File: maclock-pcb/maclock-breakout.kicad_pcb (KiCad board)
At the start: 2 copper layers, 70.5 x 26.5 mm, 10 parts, among them SW1 TS32735BK160RASMTTR, SW2 TS32735BK160RASMTTR

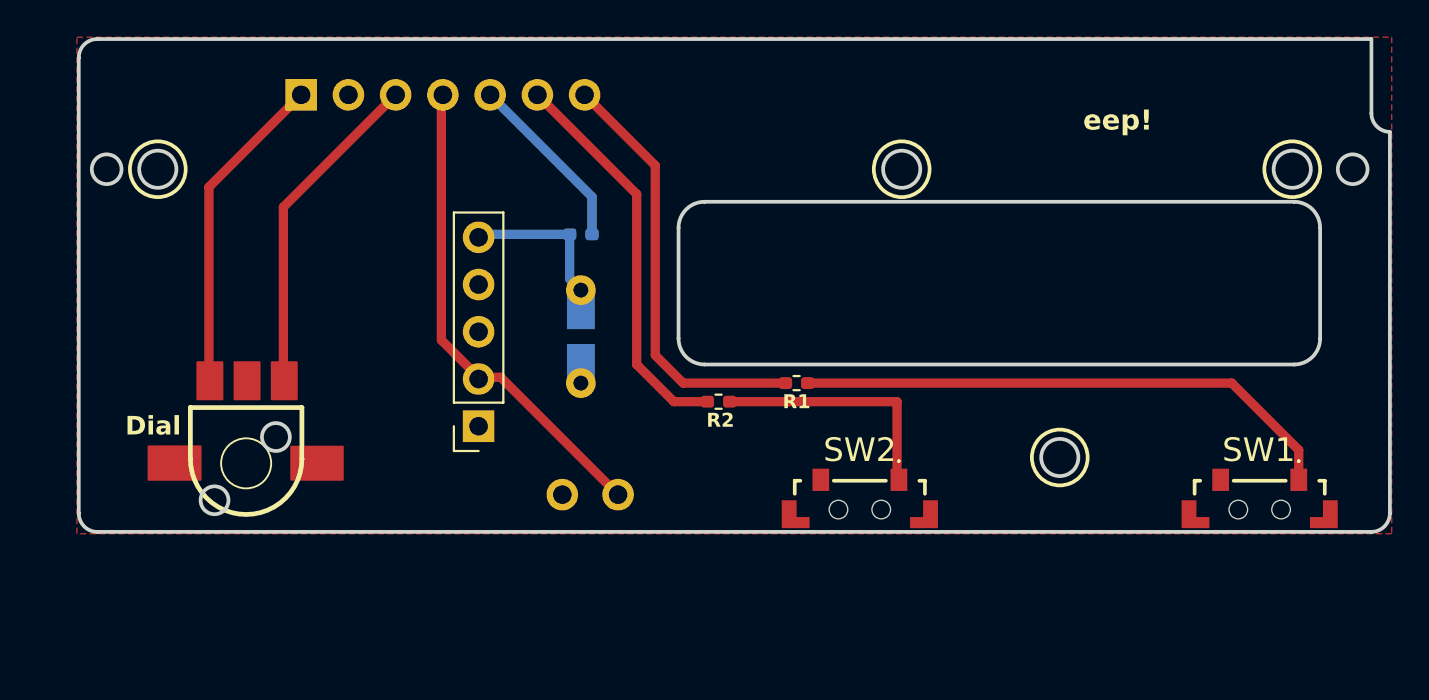
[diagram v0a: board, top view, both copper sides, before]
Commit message: PCB: real SW/encoder footprints, SMD 1206 C1, JST headers, amp decoupling
- SW1/SW2: hand-made TS32 land -> real maclock:SW_Push_5x7.8x3.8mm_SMD, same
  placement; value TS32-7-35-BK-160-RA-SMT-TR
- ENC1: fake 'Dial' copper -> real E8E8-3.2C60-9B34 encoder footprint, pads
  netted (ENC_A/ENC_B/GND)
- C1: hybrid disc/chip land now SMD-classed with a 1206 chip 3D model (100nF)
- J1/J2: JST ZH 2-pin/4-pin vertical connectors (wiring in progress)
- C2/C3: 10uF + 100nF decoupling at the PAM8302 Vin (JP1)
- README BOM updated; new maclock.pretty footprint library
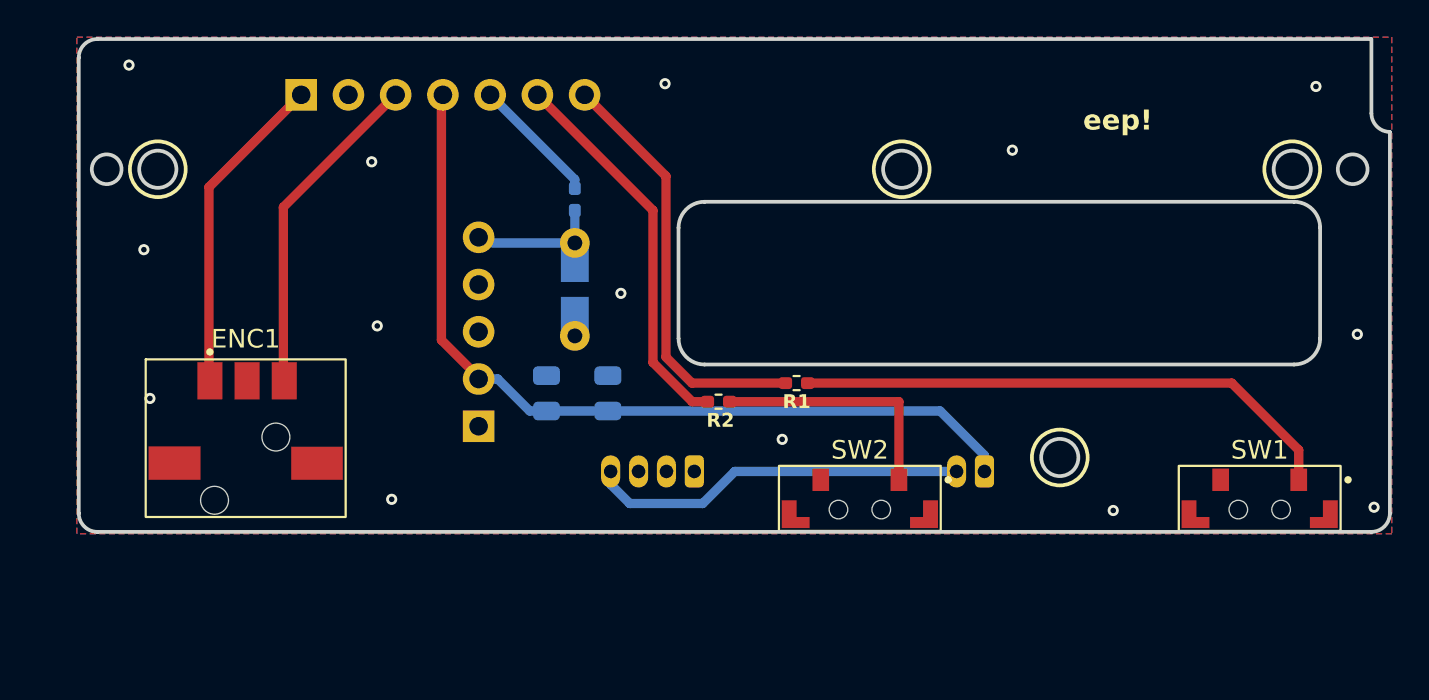
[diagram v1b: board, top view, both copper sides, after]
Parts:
- removed BAT+: 5V, 
- removed BAT-: GND, 
- added C2: 100nF, Capacitor_SMD:C_0805_2012Metric, B.Cu at (145.9, 97.0)
- added C3: 10uF, Capacitor_SMD:C_0805_2012Metric, B.Cu at (142.7, 97.0)
- added ENC1: E8E8-3.2C60-9B34, maclock:RotaryEncoder_E8E8-3.2C60-9B34_SMD, F.Cu at (126.5, 100.0)
- added J1: JST_ZH_B2B-ZR_1x02_P1.50mm_Vertical, Connector_JST:JST_ZH_B2B-ZR_1x02_P1.50mm_Vertical, B.Cu at (166.2, 101.2)
- added J2: JST_ZH_B4B-ZR_1x04_P1.50mm_Vertical, Connector_JST:JST_ZH_B4B-ZR_1x04_P1.50mm_Vertical, B.Cu at (150.6, 101.2)
- C1: footprint Capacitor_THT:C_Disc_D6.0mm_W2.5mm_P5.00mm -> maclock:C_Chip_or_Disc_P5mm_SMD
- JP1: moved to B.Cu
- SW1, SW2: value TS32735BK160RASMTTR -> TS32-7-35-BK-160-RA-SMT-TR; footprint KiCad:TS32735BK160RASMTTR -> maclock:SW_Push_5x7.8x3.8mm_SMD
- moved C1 2.56 mm to (144.2, 94.0)
- moved R3 1.90 mm to (144.2, 86.6), turned to 90 degrees
- turned JP1 to 0 degrees
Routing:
- net 5V_IN: track 0.00 -> 20.4 mm
- net 5V: track 26.1 -> 45.7 mm
- net AUDIO: track 18.1 -> 14.0 mm
- net BTN2: track 34.6 -> 34.1 mm
- net GND: vias 0 -> 14
- added copper zone on B.Cu, net GND
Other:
- outline, holes or cut-outs redrawn
- board text added: "rev 2026.09"
- board text removed: "Dial"
- board text removed: "Input"
- board text removed: "rev 2026.05"

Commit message: PCB: real HYCW03 encoder, LCSC-sourceable BOM, rebuilt schematic
- ENC1: F-Switch E8E8-3.2C60-9B34 (not on LCSC) -> HOAUC HYCW03-2.8D-5P-S
  (C55218995); new footprint, bore placed 8.8mm from the left edge / 4mm from
  the bottom to keep the dial aligned with the case
- Nets: split the series-resistor button nets (BTN1/SW1, BTN2/SW2) so each is
  fully connected; assigned ENC1 pad nets; normalized all board nets to the
  /-prefixed hierarchical form to match the schematic
- Rebuilt maclock-breakout.kicad_sch from the PCB (was a PiInput-only stub):
  all 11 parts with correct footprints/values/LCSC, custom ENC1 symbol in
  maclock.kicad_sym; ERC 0/0, board<->schematic parity clean but for benign
  symbol metadata
- BOM: every part now resolves to an LCSC number (added J1 C158011, J2 C157997);
  PCBWAY_REPLY.md answers the quote's four flagged parts
- Switches: added TS24CA and TSB001 side-switch footprints as LCSC-stocked
  alternatives to the Same Sky TS32; board left on the TS32 for hand-positioning
- scripts/: reproducible pcbnew edits (bundled Python) for each board change
- README: BOM, sourcing, J1 power switch / J2 power input, schematic status
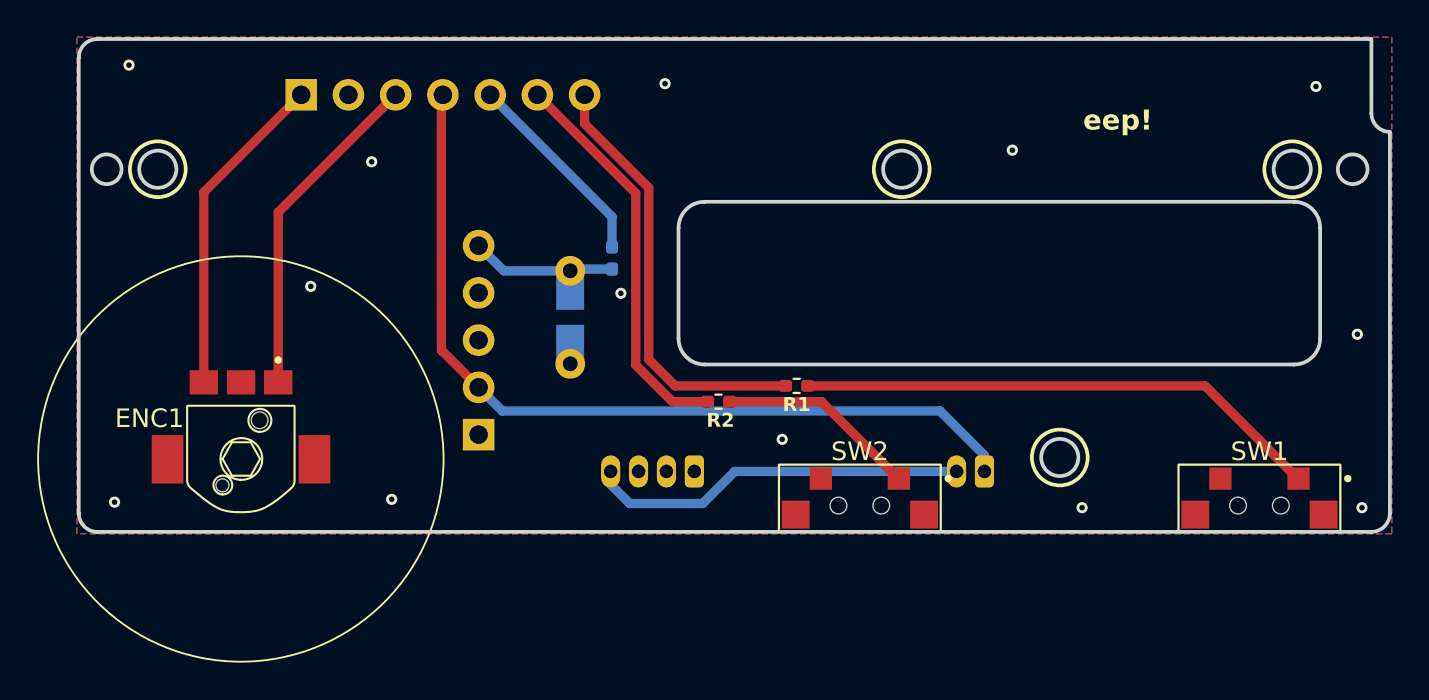
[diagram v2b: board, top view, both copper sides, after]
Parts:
- removed C2: 100nF, Capacitor_SMD:C_0805_2012Metric
- removed C3: 10uF, Capacitor_SMD:C_0805_2012Metric
- ENC1: value E8E8-3.2C60-9B34 -> HYCW03-2.8D-5P-S; footprint maclock:RotaryEncoder_E8E8-3.2C60-9B34_SMD -> maclock:RotaryEncoder_HYCW03-2.8D-5P-S_SMD
- JP1: value Rotary_Encoder_5pin -> PAM8302_Socket_1x5
- SW1, SW2: value TS32-7-35-BK-160-RA-SMT-TR -> SW_TSB001_7.7x3.55_SideSMD; footprint maclock:SW_Push_5x7.8x3.8mm_SMD -> maclock:SW_TSB001_7.7x3.55_SideSMD
- moved R3 3.73 mm to (146.2, 89.8), turned to -90 degrees
- moved SW1 1.65 mm to (181.0, 102.6)
- moved SW2 1.64 mm to (159.5, 102.6)
- moved C1 1.52 mm to (143.9, 95.5)
- moved ENC1 1.50 mm to (126.2, 98.5), turned to 180 degrees
- moved JP1 0.45 mm to (139.0, 99.3)
- moved R1 0.15 mm to (156.1, 96.7)
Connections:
- net 5V renamed /5V
- net 5V_IN renamed /5V_IN
- C1 pad 1: GND -> /GND
- C1 pad 2: AUDIO -> /A+
- ENC1 pad 4: GND -> /GND
- ENC1 pad 5: GND -> /GND
- J2 pad 3: GND -> /GND
- JP1 pad 1: GND -> /GND
- JP1 pad 4: GND -> /GND
- JP1 pad 5: AUDIO -> /A+
- PiInput pad 1: ENC_B -> /ENC_B
- PiInput pad 2: GND -> /GND
- PiInput pad 3: ENC_A -> /ENC_A
- PiInput pad 5: AUDIO -> /AUDIO
- PiInput pad 6: BTN2 -> /BTN2
- PiInput pad 7: BTN1 -> /BTN1
- R1 pad 1: BTN1 -> /BTN1
- R1 pad 2: BTN1 -> /SW1
- R2 pad 1: BTN2 -> /BTN2
- R2 pad 2: BTN2 -> /SW2
- R3 pad 1: AUDIO -> /AUDIO
- R3 pad 2: AUDIO -> /A+
- SW1 pad 1: BTN1 -> /SW1
- SW1 pad 2: GND -> /GND
- SW1 pad 3: GND -> /GND
- SW1 pad 4: GND -> /GND
- SW2 pad 1: BTN2 -> /SW2
- SW2 pad 2: GND -> /GND
- SW2 pad 3: GND -> /GND
- SW2 pad 4: GND -> /GND
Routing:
- net BTN1: track 52.4 -> 0.00 mm
- net BTN2: track 34.1 -> 0.00 mm
- net /SW1: track 0.00 -> 28.3 mm
- net /BTN1: track 0.00 -> 23.6 mm
- net /BTN2: track 0.00 -> 21.4 mm
- net /ENC_A: track 0.00 -> 18.1 mm
- net /ENC_B: track 0.00 -> 17.6 mm
- net ENC_A: track 17.5 -> 0.00 mm
- net ENC_B: track 17.1 -> 0.00 mm
- net AUDIO: track 14.0 -> 0.00 mm
- net /AUDIO: track 0.00 -> 10.9 mm
- net /SW2: track 0.00 -> 10.8 mm
- net /A+: track 0.00 -> 7.77 mm
- net GND: vias 14 -> 0
- net /GND: vias 0 -> 13
- added copper zone on B.Cu, net /GND
- added copper zone on F.Cu, net /GND
- removed copper zone on B.Cu, net GND
- removed copper zone on F.Cu, net GND
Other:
- board text added: "by Wells Workshop - https://wells.ee"
- board text removed: "Designed by Wells Riley •https://wells.ee"

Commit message: PCB: TSB001 part numbers on board, C1 10nF audio LPF, J2 polarity silk, project lib tables, C1 1206 model
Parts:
- C1: value 100nF -> 10nF
- SW1, SW2: value SW_TSB001_7.7x3.55_SideSMD -> TSB001A3518A
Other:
- board text added: "+"
- board text added: "-"
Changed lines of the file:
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@@
 			)
 		)
-		(property "Value" "SW_TSB001_7.7x3.55_SideSMD"
+		(property "Value" "TSB001A3518A"
 			(at 0 2.82 0)
 			(layer "F.Fab")
@@
 			)
 		)
+		(property "LCSC" "C2888448"
+			(at 0 0 0)
+			(layer "F.SilkS")
+			(hide yes)
+			(effects
+				(font
+					(size 1.27 1.27)
+					(thickness 0.15)
+				)
+			)
+		)
 		(attr smd)
 		(duplicate_pad_numbers_are_jumpers no)
@@
 			)
 		)
-		(property "Value" "SW_TSB001_7.7x3.55_SideSMD"
+		(property "Value" "TSB001A3518A"
 			(at 0 2.82 0)
 			(layer "F.Fab")
@@
 			)
 		)
+		(property "LCSC" "C2888448"
+			(at 0 0 0)
+			(layer "F.SilkS")
+			(hide yes)
+			(effects
+				(font
+					(size 1.27 1.27)
+					(thickness 0.15)
+				)
+			)
+		)
 		(attr smd)
 		(duplicate_pad_numbers_are_jumpers no)
@@
 			)
 		)
-		(property "Value" "100nF"
+		(property "Value" "10nF"
 			(at 2.5 -2.05 270)
 			(layer "B.Fab")
@@
 			)
 		)
-		(property "LCSC" "C24497"
+		(property "LCSC" "C1846"
 			(at 0 0 0)
 			(layer "B.SilkS")
@@
 		)
 		(embedded_fonts no)
-		(model "${KICAD9_3DMODEL_DIR}/Capacitor_SMD.3dshapes/C_0402_1005Metric.step"
+		(model "${KICAD10_3DMODEL_DIR}/Capacitor_SMD.3dshapes/C_1206_3216Metric.step"
 			(offset
 				(xyz 2.5 0 0)
@@
 		)
 	)
+	(gr_text "+"
+		(at 146.1 99.15 0)
+		(layer "B.SilkS")
+		(effects
+			(font
+				(size 0.8 0.8)
+				(thickness 0.15)
+			)
+			(justify mirror)
+		)
+	)
+	(gr_text "-"
+		(at 147.6 99.15 0)
+		(layer "B.SilkS")
+		(effects
+			(font
+				(size 0.8 0.8)
+				(thickness 0.15)
+			)
+			(justify mirror)
+		)
+	)
 	(gr_text "Pi GPIO"
 		(at 127.5 81 0)
@@
 		(layer "B.SilkS")
 	)
+	(segment
+		(start 178.0625 96.65)
+		(end 156.845 96.65)
+		(width 0.5)
+		(layer "F.Cu")
+		(net "/SW1")
+	)
+	(segment
+		(start 183.0875 101.675)
+		(end 178.0625 96.65)
+		(width 0.5)
+		(layer "F.Cu")
+		(net "/SW1")
+	)
 	(via
 		(at 186.25 93.875)
@@
 	)
 	(segment
+		(start 152.5 97.5)
+		(end 157.445 97.5)
+		(width 0.5)
+		(layer "F.Cu")
+		(net "/SW2")
+	)
+	(segment
+		(start 157.445 97.5)
+		(end 161.6 101.655)
+		(width 0.5)
+		(layer "F.Cu")
+		(net "/SW2")
+	)
+	(segment
 		(start 149.425 97.5)
 		(end 151.305 97.5)
@@
 	)
 	(segment
-		(start 152.5 97.5)
-		(end 157.445 97.5)
-		(width 0.5)
-		(layer "F.Cu")
-		(net "/SW2")
-	)
-	(segment
-		(start 157.445 97.5)
-		(end 161.6 101.655)
-		(width 0.5)
-		(layer "F.Cu")
-		(net "/SW2")
-	)
-	(segment
-		(start 178.0625 96.65)
-		(end 156.845 96.65)
-		(width 0.5)
-		(layer "F.Cu")
-		(net "/SW1")
-	)
-	(segment
-		(start 183.0875 101.675)
-		(end 178.0625 96.65)
-		(width 0.5)
-		(layer "F.Cu")
-		(net "/SW1")
-	)
-	(segment

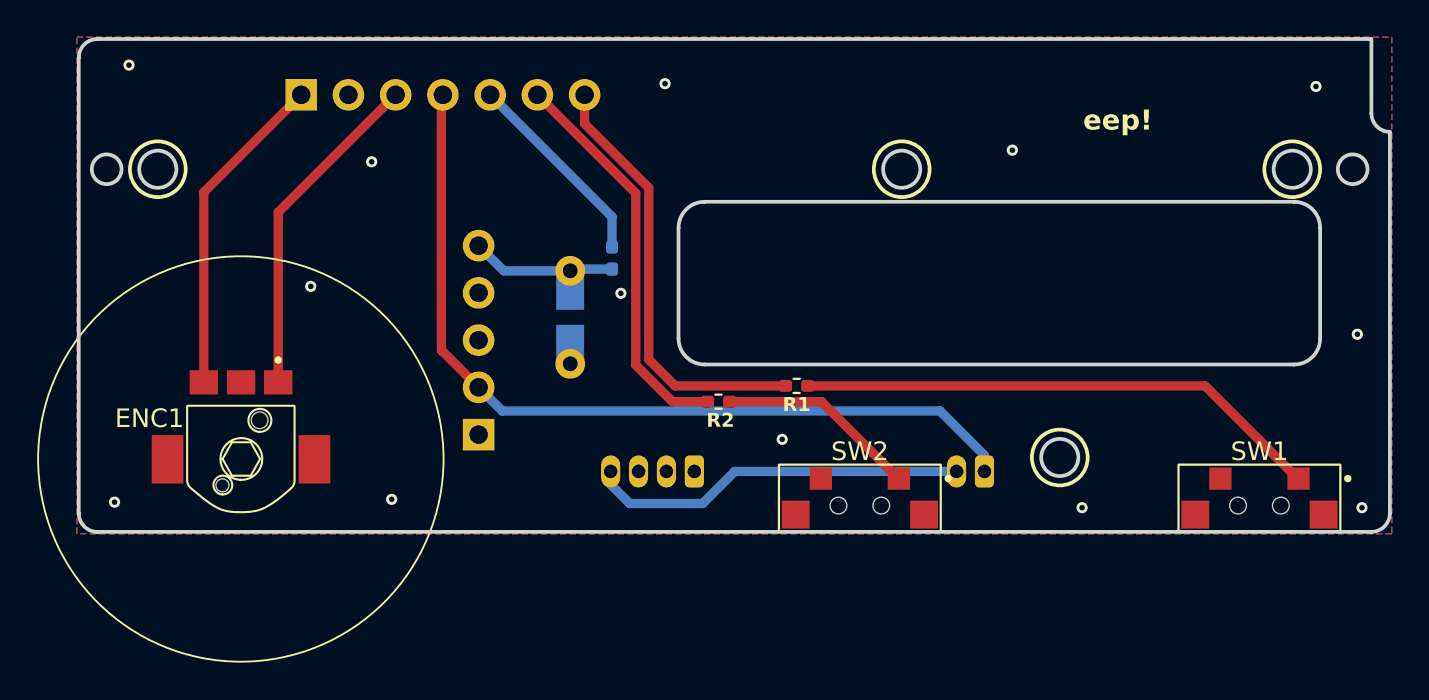
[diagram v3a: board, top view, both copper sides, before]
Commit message: PCB: connector MPN values, 1.0 mm 5V supply tracks
- J1/J2/JP1/PiInput Value -> B2B-ZR(LF)(SN) / B4B-ZR(LF)(SN) / 2.54-1*5PFemale / PZ254V-11-07P
  on board and schematic (PCBway reads the board's Value column)
- /5V and /5V_IN tracks 0.5 -> 1.0 mm; the J2 pad-1 skirt is 0.8 mm and the diagonal out of
  JP1 pin 2 stays 0.5 mm (2.54 mm socket pitch); long y=98 run restarted at x=141 with a stub
  so its round end clears JP1 pin 1 (GND)
- DRC 0 errors / 0 unconnected; ERC 0; scripts/mpn_values_and_wide_5v.py
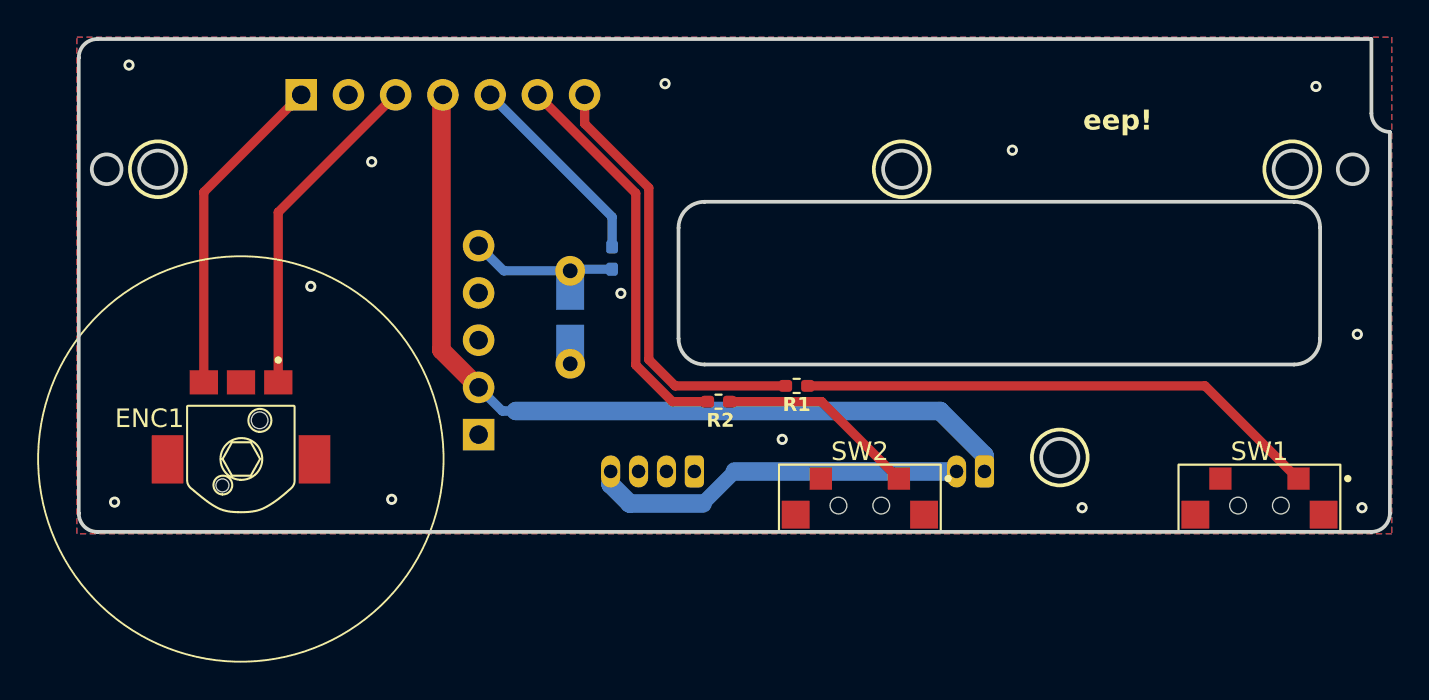
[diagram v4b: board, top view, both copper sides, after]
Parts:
- J1: value JST_ZH_B2B-ZR_1x02_P1.50mm_Vertical -> B2B-ZR(LF)(SN)
- J2: value JST_ZH_B4B-ZR_1x04_P1.50mm_Vertical -> B4B-ZR(LF)(SN)
- JP1: value PAM8302_Socket_1x5 -> 2.54-1*5PFemale
- PiInput: value PinHeader_1x07_P2.54mm_Vertical -> PZ254V-11-07P
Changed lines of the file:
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@@
 			)
 		)
-		(property "Value" "PAM8302_Socket_1x5"
+		(property "Value" "2.54-1*5PFemale"
 			(at 0 -12.93 0)
 			(layer "B.Fab")
@@
 			)
 		)
-		(property "Value" "JST_ZH_B2B-ZR_1x02_P1.50mm_Vertical"
+		(property "Value" "B2B-ZR(LF)(SN)"
 			(at 0.75 -3.4 0)
 			(unlocked yes)
@@
 			)
 		)
-		(property "Value" "JST_ZH_B4B-ZR_1x04_P1.50mm_Vertical"
+		(property "Value" "B4B-ZR(LF)(SN)"
 			(at 2.25 -3.4 0)
 			(unlocked yes)
@@
 			)
 		)
-		(property "Value" "PinHeader_1x07_P2.54mm_Vertical"
+		(property "Value" "PZ254V-11-07P"
 			(at 0 -17.62 90)
 			(layer "B.Fab")
@@
 		(start 137 81.08)
 		(end 137 94.73)
-		(width 0.5)
+		(width 1)
 		(layer "F.Cu")
 		(net "/5V")
@@
 		(start 137 94.73)
 		(end 139 96.73)
-		(width 0.5)
+		(width 1)
 		(layer "F.Cu")
 		(net "/5V")
@@
 		(start 166.2 100.385)
 		(end 166.2 101.25)
-		(width 0.5)
+		(width 1)
 		(layer "B.Cu")
 		(net "/5V")
 	)
 	(segment
-		(start 140.27 98)
+		(start 141 98)
 		(end 163.815 98)
-		(width 0.5)
+		(width 1)
 		(layer "B.Cu")
 		(net "/5V")
@@
 		(start 163.815 98)
 		(end 166.2 100.385)
+		(width 1)
+		(layer "B.Cu")
+		(net "/5V")
+	)
+	(segment
+		(start 140.27 98)
+		(end 141 98)
 		(width 0.5)
 		(layer "B.Cu")
@@
 		(start 152.775 101.25)
 		(end 151.05 102.975)
-		(width 0.5)
+		(width 0.8)
 		(layer "B.Cu")
 		(net "/5V_IN")
@@
 		(start 147.125 102.975)
 		(end 146.1 101.95)
-		(width 0.5)
+		(width 1)
 		(layer "B.Cu")
 		(net "/5V_IN")
@@
 		(start 164.7 101.25)
 		(end 152.775 101.25)
-		(width 0.5)
+		(width 1)
 		(layer "B.Cu")
 		(net "/5V_IN")
@@
 		(start 146.1 101.95)
 		(end 146.1 101.25)
-		(width 0.5)
+		(width 1)
 		(layer "B.Cu")
 		(net "/5V_IN")
@@
 		(start 151.05 102.975)
 		(end 147.125 102.975)
-		(width 0.5)
+		(width 1)
 		(layer "B.Cu")
 		(net "/5V_IN")
